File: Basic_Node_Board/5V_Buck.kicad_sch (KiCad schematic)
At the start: 13 parts, among them J2 Conn_01x02, U1 TPS54560BQDDARQ1

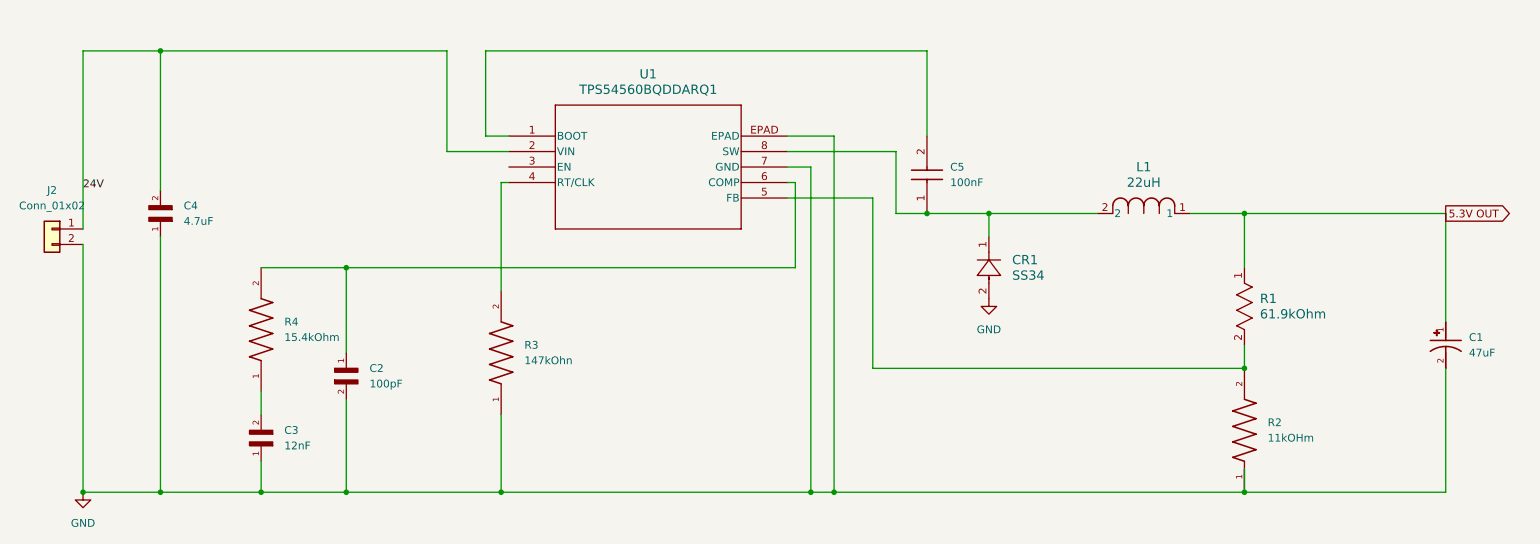
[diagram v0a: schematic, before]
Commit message: updated telem pcb, will do mcu next on this branch. Key actions: corrected ground plane to make it a plane, not a few wires, which is important for heat disipation. I made the Vcc plane another ground plane instead, since it wasnt really necessary for Vcc, and a second gnd plane should better help with heat. I also did not extend the ground plane under the ebyte, since their instructions say to avoid routing power underneath. Its a bit confusing, since there appear to be some pads under the module for gnd that we arent using. ive heard that having a gnd plane under rf module can create problematic couping, so would rather be safe and do this, should still be plenty able to dissipate heat without it. the inductor and diode for the buck converter were both too small. The inductor had double the ESR of the suggested TI on, so likely wouldnt be great. The diode would never survive the buck converter. The diode i am using is the one TI suggested from the web-bench, and is considerabley larger, and rated for 5 Amps. This is important for a 2A buck. The diode often temporarily has to more than the bucks output. Also updated the CAN Controller (the TJA...) I think the circuit that was being used there was intended as a test circuit, not an implementation. we would never want to add extra capacitacne on CANH and CANL, i think those capacitors were for testing the modules ability to drive a network. The new CAN circuit is now just an optional termination resistor, and a local capacitor between gnd and Vcc. I removed partslib, and other parts that were added here. all parts (symbols, footprints, 3D stuff) should go in the seperate partslib repo. I suggest cloning partslib adjascent to your pcb directory, and then setting up your kicad paths appropriately (will write a memo on this later)
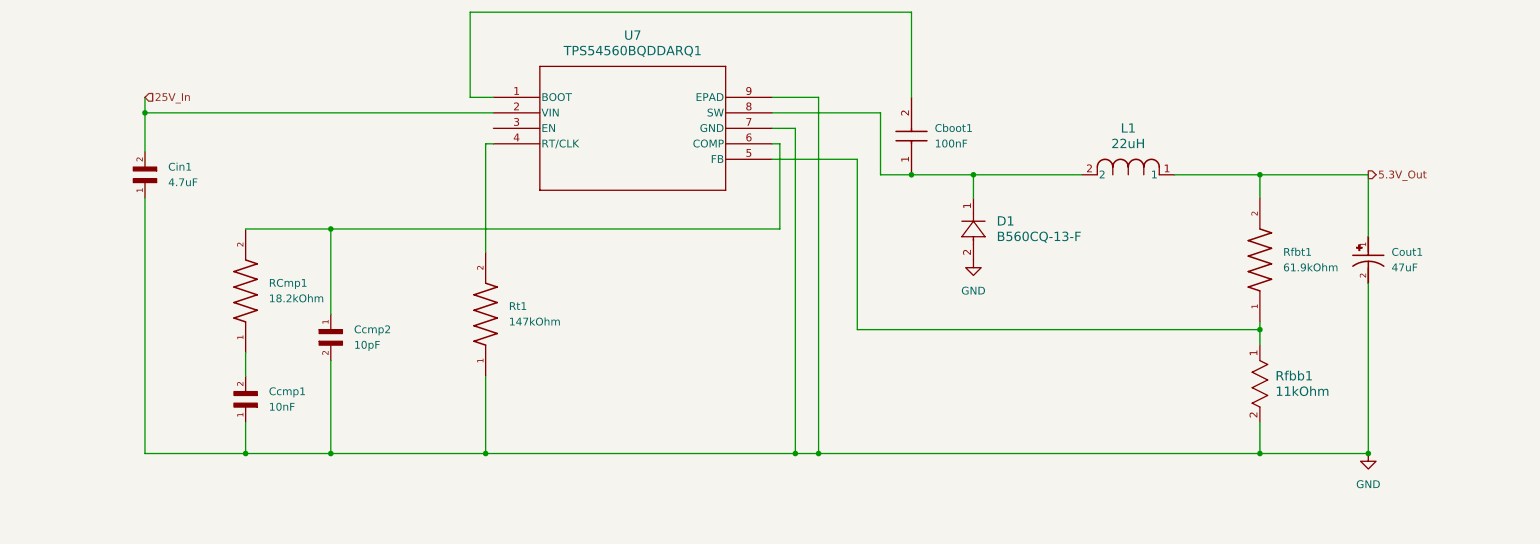
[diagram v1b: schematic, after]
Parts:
- removed C1: 47uF, Capacitor_SMD:C_0402_1005Metric_Pad0.74x0.62mm_HandSolder, symbol 10TPE47MAZB:10TPE47MAZB
- removed C2: 100pF, Capacitor_SMD:C_0603_1608Metric_Pad1.08x0.95mm_HandSolder, symbol CL05C110JB5NNNC:CL05C110JB5NNNC
- removed C3: 12nF, Capacitor_SMD:C_0504_1310Metric_Pad0.83x1.28mm_HandSolder, symbol C0805C122J5GACTU:C0805C122J5GACTU
- removed C4: 4.7uF, Capacitor_SMD:C_0504_1310Metric_Pad0.83x1.28mm_HandSolder, symbol GRM31CR71H475KA12L:GRM31CR71H475KA12L
- removed C5: 100nF, Capacitor_SMD:C_0504_1310Metric_Pad0.83x1.28mm_HandSolder, symbol 08053C104KAT2A:08053C104KAT2A
- removed CR1: SS34, Diode_SMD:D_0201_0603Metric_Pad0.64x0.40mm_HandSolder, symbol B560C-13-F:B560C-13-F
- removed J2: Conn_01x02, Connector_PinHeader_2.54mm:PinHeader_1x04_P2.54mm_Vertical, symbol Connector_Generic:Conn_01x02
- removed R1: 61.9kOhm, Resistor_SMD:R_0201_0603Metric_Pad0.64x0.40mm_HandSolder, symbol 2026-02-07_22-08-15:CRCW040261K9FKED
- removed R2: 11kOHm, Resistor_SMD:R_0201_0603Metric_Pad0.64x0.40mm_HandSolder, symbol CRCW040211K0FKED:CRCW040211K0FKED
- removed R3: 147kOhn, Resistor_SMD:R_0201_0603Metric_Pad0.64x0.40mm_HandSolder, symbol CRCW0402118KFKED:CRCW0402118KFKED
- removed R4: 15.4kOhm, Resistor_SMD:R_0201_0603Metric_Pad0.64x0.40mm_HandSolder, symbol RC0201FR-0723K7L:RC0201FR-0723K7L
- removed U1: TPS54560BQDDARQ1, PROVE-footprints:VREG_LM5017MR_NOPB, symbol TPS54560BQDDARQ1:TPS54560BQDDARQ1
- added Cboot1: 100nF, Capacitor_SMD:C_1206_3216Metric_Pad1.33x1.80mm_HandSolder, symbol 08053C104KAT2A:08053C104KAT2A
- added Ccmp1: 10nF, Capacitor_SMD:C_1206_3216Metric_Pad1.33x1.80mm_HandSolder, symbol C0805C122J5GACTU:C0805C122J5GACTU
- added Ccmp2: 10pF, Capacitor_SMD:C_1206_3216Metric_Pad1.33x1.80mm_HandSolder, symbol CL05C110JB5NNNC:CL05C110JB5NNNC
- added Cin1: 4.7uF, Capacitor_SMD:C_1206_3216Metric_Pad1.33x1.80mm_HandSolder, symbol GRM31CR71H475KA12L:GRM31CR71H475KA12L
- added Cout1: 47uF, Capacitor_Tantalum_SMD:CP_EIA-3528-21_Kemet-B_HandSolder, symbol 10TPE47MAZB:10TPE47MAZB
- added D1: B560CQ-13-F, Diode_SMD:D_SMC, symbol B560C-13-F:B560C-13-F
- added RCmp1: 18.2kOhm, Resistor_SMD:R_1206_3216Metric_Pad1.30x1.75mm_HandSolder, symbol RC0201FR-0723K7L:RC0201FR-0723K7L
- added Rfbb1: 11kOhm, Resistor_SMD:R_1206_3216Metric_Pad1.30x1.75mm_HandSolder, symbol 2026-02-07_22-08-15:CRCW040261K9FKED
- added Rfbt1: 61.9kOhm, Resistor_SMD:R_1206_3216Metric_Pad1.30x1.75mm_HandSolder, symbol CRCW040211K0FKED:CRCW040211K0FKED
- added Rt1: 147kOhm, Resistor_SMD:R_1206_3216Metric_Pad1.30x1.75mm_HandSolder, symbol CRCW0402118KFKED:CRCW0402118KFKED
- added U7: TPS54560BQDDARQ1, Package_SO:SOIC-8-1EP_3.9x4.9mm_P1.27mm_EP2.29x3mm, symbol TPS54560BQDDARQ1:TPS54560BQDDARQ1
- L1: footprint Inductor_SMD:L_0201_0603Metric_Pad0.64x0.40mm_HandSolder -> Inductor_SMD:L_Bourns_SRP1245A; Purchase Link (none) -> https://www.mouser.com/en/ProductDetail/Bourns/SRP1265A-220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; Specs (none) -> L: 22 µH DCR: 37 mΩ IDC: 9 A
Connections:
- net GND: now also Ccmp1.1, Ccmp2.2, Cin1.1, Cout1.2, D1.2, Rfbb1.2, Rt1.1, U7.7 (GND), U7.9 (EPAD)
- net at L1.2: now also Cboot1.1, D1.1, U7.8 (SW)
- net 5.3V OUT renamed 5.3V_Out
- net 5.3V_Out: now also Cout1.1, Rfbt1.2
- new net: Cboot1.2, U7.1 (BOOT)
- new net: Rt1.2, U7.4 (RT/CLK)
- new net: Rfbb1.1, Rfbt1.1, U7.5 (FB)
- new net: Ccmp2.1, RCmp1.2, U7.6 (COMP)
- new net: Ccmp1.2, RCmp1.1
- new net 25V_In: Cin1.2, U7.2 (VIN)
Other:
- company: PROVE Lab - Low Voltage -> (none)
- title: 24V_to_5.3_Buck_Converter -> (none)
